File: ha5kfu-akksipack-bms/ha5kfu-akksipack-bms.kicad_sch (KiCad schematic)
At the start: 51 parts, among them IC2 BQ4050RSMR, J1 PACK, J2 PACK1, J3 PACK2, J4 COM, Q1 AON6512, Q2 AON6512, Q3 2N7002, Q4 AO3400A, Q5 AO3400A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

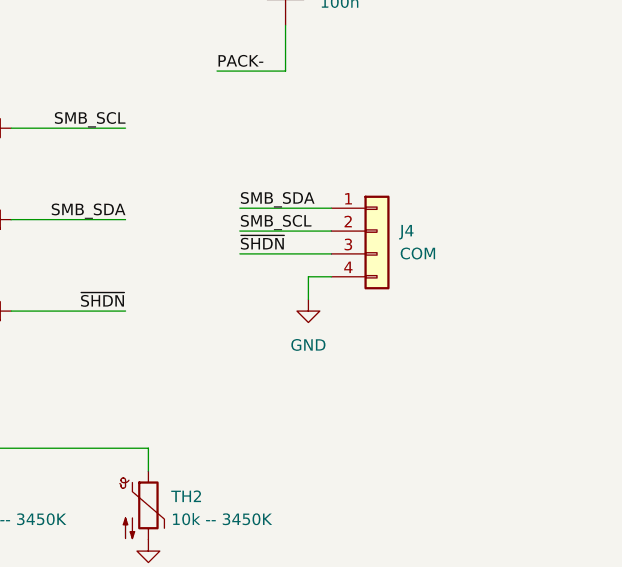
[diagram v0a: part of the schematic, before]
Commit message: Add pull-down for /SHDN
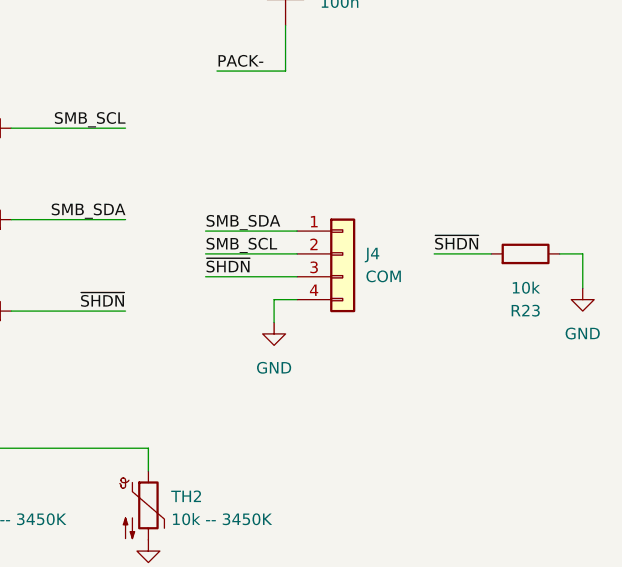
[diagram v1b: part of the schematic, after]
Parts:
- added R23: 10k, Resistor_SMD:R_0805_2012Metric_Pad1.20x1.40mm_HandSolder, symbol Device:R
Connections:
- net GND: now also R23.1
- net ~{SHDN}: now also R23.2
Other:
- moved on the sheet: J4
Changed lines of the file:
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@@
 	(wire
 		(pts
-			(xy 238.76 113.03) (xy 248.92 113.03)
+			(xy 234.95 115.57) (xy 245.11 115.57)
 		)
 		(stroke
@@
 	(wire
 		(pts
+			(xy 276.86 116.84) (xy 276.86 113.03)
+		)
+		(stroke
+			(width 0)
+			(type default)
+		)
+	)
+	(wire
+		(pts
 			(xy 36.83 73.66) (xy 36.83 91.44)
 		)
@@
 	(wire
 		(pts
-			(xy 246.38 118.11) (xy 246.38 115.57)
+			(xy 242.57 120.65) (xy 242.57 118.11)
 		)
 		(stroke
@@
 	(wire
 		(pts
+			(xy 266.7 113.03) (xy 260.35 113.03)
+		)
+		(stroke
+			(width 0)
+			(type default)
+		)
+	)
+	(wire
+		(pts
 			(xy 191.77 43.18) (xy 186.69 43.18)
 		)
@@
 	(wire
 		(pts
-			(xy 246.38 115.57) (xy 248.92 115.57)
+			(xy 242.57 118.11) (xy 245.11 118.11)
 		)
 		(stroke
@@
 	(wire
 		(pts
-			(xy 238.76 110.49) (xy 248.92 110.49)
+			(xy 234.95 113.03) (xy 245.11 113.03)
 		)
 		(stroke
@@
 	(wire
 		(pts
-			(xy 238.76 107.95) (xy 248.92 107.95)
+			(xy 234.95 110.49) (xy 245.11 110.49)
 		)
 		(stroke
@@
 	(wire
 		(pts
+			(xy 276.86 113.03) (xy 274.32 113.03)
+		)
+		(stroke
+			(width 0)
+			(type default)
+		)
+	)
+	(wire
+		(pts
 			(xy 90.17 111.76) (xy 90.17 119.38)
 		)
@@
 	)
 	(label "SMB_SCL"
-		(at 238.76 110.49 0)
+		(at 234.95 113.03 0)
 		(effects
 			(font
@@
 	)
 	(label "SMB_SDA"
-		(at 238.76 107.95 0)
+		(at 234.95 110.49 0)
 		(effects
 			(font
@@
 		)
 	)
+	(label "~{SHDN}"
+		(at 260.35 113.03 0)
+		(effects
+			(font
+				(size 1.27 1.27)
+			)
+			(justify left bottom)
+		)
+	)
 	(label "SMB_SDA"
 		(at 226.06 109.22 180)
@@
 	)
 	(label "~{SHDN}"
-		(at 238.76 113.03 0)
+		(at 234.95 115.57 0)
 		(effects
 			(font
@@
 	(symbol
 		(lib_id "power:GND")
-		(at 246.38 118.11 0)
+		(at 242.57 120.65 0)
 		(unit 1)
 		(exclude_from_sim no)
@@
 		(fields_autoplaced yes)
 		(property "Reference" "#PWR09"
-			(at 246.38 124.46 0)
+			(at 242.57 127 0)
 			(effects
 				(font
@@
 		)
 		(property "Value" "GND"
-			(at 246.38 123.19 0)
+			(at 242.57 125.73 0)
 			(effects
 				(font
@@
 		)
 		(property "Footprint" ""
-			(at 246.38 118.11 0)
+			(at 242.57 120.65 0)
 			(effects
 				(font
@@
 		)
 		(property "Datasheet" ""
-			(at 246.38 118.11 0)
+			(at 242.57 120.65 0)
 			(effects
 				(font
@@
 		)
 		(property "Description" "Power symbol creates a global label with name \"GND\" , ground"
-			(at 246.38 118.11 0)
+			(at 242.57 120.65 0)
 			(effects
 				(font
@@
 	)
 	(symbol
+		(lib_id "power:GND")
+		(at 276.86 116.84 0)
+		(mirror y)
+		(unit 1)
+		(exclude_from_sim no)
+		(in_bom yes)
+		(on_board yes)
+		(dnp no)
+		(fields_autoplaced yes)
+		(property "Reference" "#PWR010"
+			(at 276.86 123.19 0)
+			(effects
+				(font
+					(size 1.27 1.27)
+				)
+				(hide yes)
+			)
+		)
+		(property "Value" "GND"
+			(at 276.86 121.92 0)
+			(effects
+				(font
+					(size 1.27 1.27)
+				)
+			)
+		)
+		(property "Footprint" ""
+			(at 276.86 116.84 0)
+			(effects
+				(font
+					(size 1.27 1.27)
+				)
+				(hide yes)
+			)
+		)
+		(property "Datasheet" ""
+			(at 276.86 116.84 0)
+			(effects
+				(font
+					(size 1.27 1.27)
+				)
+				(hide yes)
+			)
+		)
+		(property "Description" "Power symbol creates a global label with name \"GND\" , ground"
+			(at 276.86 116.84 0)
+			(effects
+				(font
+					(size 1.27 1.27)
+				)
+				(hide yes)
+			)
+		)
+		(pin "1"
+		)
+		(instances
+			(project "ha5kfu-akksipack-bms"
+				(path "/9e1c3fa4-5fbe-43ed-babf-081bbfb08ec5"
+					(reference "#PWR010")
+					(unit 1)
+				)
+			)
+		)
+	)
+	(symbol
 		(lib_id "Device:D_Schottky")
 		(at 140.97 77.47 270)
@@
 	(symbol
 		(lib_id "Device:R")
+		(at 270.51 113.03 270)
+		(mirror x)
+		(unit 1)
+		(exclude_from_sim no)
+		(in_bom yes)
+		(on_board yes)
+		(dnp no)
+		(property "Reference" "R23"
+			(at 270.51 119.38 90)
+			(effects
+				(font
+					(size 1.27 1.27)
+				)
+			)
+		)
+		(property "Value" "10k"
+			(at 270.51 116.84 90)
+			(effects
+				(font
+					(size 1.27 1.27)
+				)
+			)
+		)
+		(property "Footprint" "Resistor_SMD:R_0805_2012Metric_Pad1.20x1.40mm_HandSolder"
+			(at 270.51 114.808 90)
+			(effects
+				(font
+					(size 1.27 1.27)
+				)
+				(hide yes)
+			)
+		)
+		(property "Datasheet" "~"
+			(at 270.51 113.03 0)
+			(effects
+				(font
+					(size 1.27 1.27)
+				)
+				(hide yes)
+			)
+		)
+		(property "Description" "Resistor"
+			(at 270.51 113.03 0)
+			(effects
+				(font
+					(size 1.27 1.27)
+				)
+				(hide yes)
+			)
+		)
+		(pin "1"
+		)
+		(pin "2"
+		)
+		(instances
+			(project "ha5kfu-akksipack-bms"
+				(path "/9e1c3fa4-5fbe-43ed-babf-081bbfb08ec5"
+					(reference "R23")
+					(unit 1)
+				)
+			)
+		)
+	)
+	(symbol
+		(lib_id "Device:R")
 		(at 64.77 55.88 0)
 		(unit 1)
@@
 	(symbol
 		(lib_id "Connector_Generic:Conn_01x04")
-		(at 254 110.49 0)
+		(at 250.19 113.03 0)
 		(unit 1)
 		(exclude_from_sim no)
@@
 		(fields_autoplaced yes)
 		(property "Reference" "J4"
-			(at 256.54 110.4899 0)
+			(at 252.73 113.0299 0)
 			(effects
 				(font
@@
 		)
 		(property "Value" "COM"
-			(at 256.54 113.0299 0)
+			(at 252.73 115.5699 0)
 			(effects
 				(font
@@
 		)
 		(property "Footprint" "Connector_PinHeader_2.54mm:PinHeader_1x04_P2.54mm_Vertical"
-			(at 254 110.49 0)
+			(at 250.19 113.03 0)
 			(effects
 				(font
@@
 		)
 		(property "Datasheet" "~"
-			(at 254 110.49 0)
+			(at 250.19 113.03 0)
 			(effects
 				(font
@@
 		)
 		(property "Description" "Generic connector, single row, 01x04, script generated (kicad-library-utils/schlib/autogen/connector/)"
-			(at 254 110.49 0)
+			(at 250.19 113.03 0)
 			(effects
 				(font

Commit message: Add initial PCB design
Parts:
- C1, C2, C3, C4, C5, C6, C7, C8: footprint Capacitor_SMD:C_0805_2012Metric_Pad1.18x1.45mm_HandSolder -> Capacitor_SMD:C_0603_1608Metric_Pad1.08x0.95mm_HandSolder
- C10: renamed from 100n1; value C -> 100n; footprint Capacitor_SMD:C_0805_2012Metric_Pad1.18x1.45mm_HandSolder -> Capacitor_SMD:C_0603_1608Metric_Pad1.08x0.95mm_HandSolder
- IC1: renamed from IC2; footprint BQ4050:QFN40P400X400X100-33N-D -> Package_DFN_QFN:VQFN-32-1EP_4x4mm_P0.4mm_EP2.8x2.8mm
- J1: footprint Connector_Wire:SolderWire-0.75sqmm_1x02_P4.8mm_D1.25mm_OD2.3mm -> Connector_AMASS:AMASS_XT30PW-M_1x02_P2.50mm_Horizontal
- J2, J3: footprint Connector_JST:JST_PH_B3B-PH-K_1x03_P2.00mm_Vertical -> Connector_JST:JST_PH_S3B-PH-K_1x03_P2.00mm_Horizontal
- R1, R10, R11, R13, R15, R16, R2, R3, R6, R7: footprint Resistor_SMD:R_0805_2012Metric_Pad1.20x1.40mm_HandSolder -> Resistor_SMD:R_0603_1608Metric_Pad0.98x0.95mm_HandSolder
- R12, R14, R17, R4, R5, R8, R9: footprint Resistor_SMD:R_1206_3216Metric -> Resistor_SMD:R_0603_1608Metric_Pad0.98x0.95mm_HandSolder
- R18: renamed from R23; footprint Resistor_SMD:R_0805_2012Metric_Pad1.20x1.40mm_HandSolder -> Resistor_SMD:R_0603_1608Metric_Pad0.98x0.95mm_HandSolder
- R19: renamed from R18; footprint Resistor_SMD:R_0805_2012Metric_Pad1.20x1.40mm_HandSolder -> Resistor_SMD:R_0603_1608Metric_Pad0.98x0.95mm_HandSolder
- R20: renamed from R19; footprint Resistor_SMD:R_1206_3216Metric -> Resistor_SMD:R_0603_1608Metric_Pad0.98x0.95mm_HandSolder
- R21: renamed from R20; footprint Resistor_SMD:R_1206_3216Metric -> Resistor_SMD:R_1206_3216Metric_Pad1.30x1.75mm_HandSolder
- R22: renamed from R21; footprint Resistor_SMD:R_0805_2012Metric_Pad1.20x1.40mm_HandSolder -> Resistor_SMD:R_0603_1608Metric_Pad0.98x0.95mm_HandSolder
- R23: renamed from R22; footprint Resistor_SMD:R_0805_2012Metric_Pad1.20x1.40mm_HandSolder -> Resistor_SMD:R_0603_1608Metric_Pad0.98x0.95mm_HandSolder
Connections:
- net GND: now also J3.1 (Pin_1); no longer J3.3 (Pin_3)
- net at BT2.2 (-), BT3.1 (+), Q5.2 (S)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: now also J2.1 (Pin_1), J3.3 (Pin_3); no longer J2.3 (Pin_3), J3.1 (Pin_1)
- net at BT1.1 (+), C1.1, D1.2 (A)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: now also J2.3 (Pin_3); no longer J2.1 (Pin_1)
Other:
- moved on the sheet: J2, J3

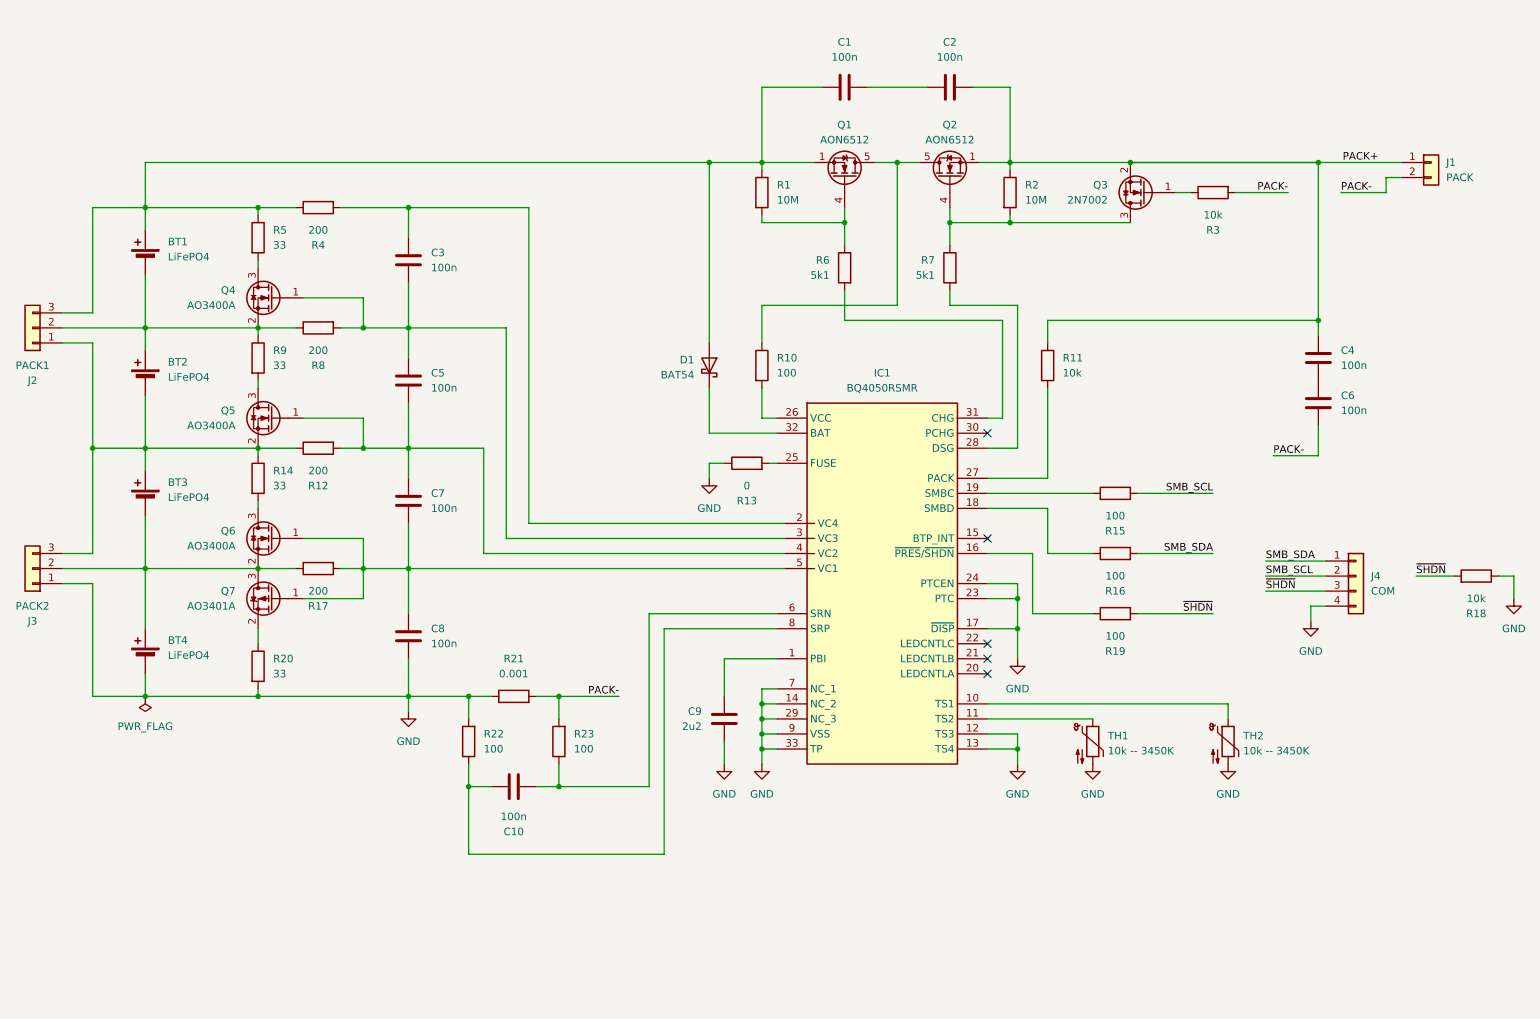
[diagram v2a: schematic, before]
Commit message: Add LEDs, modify PCB
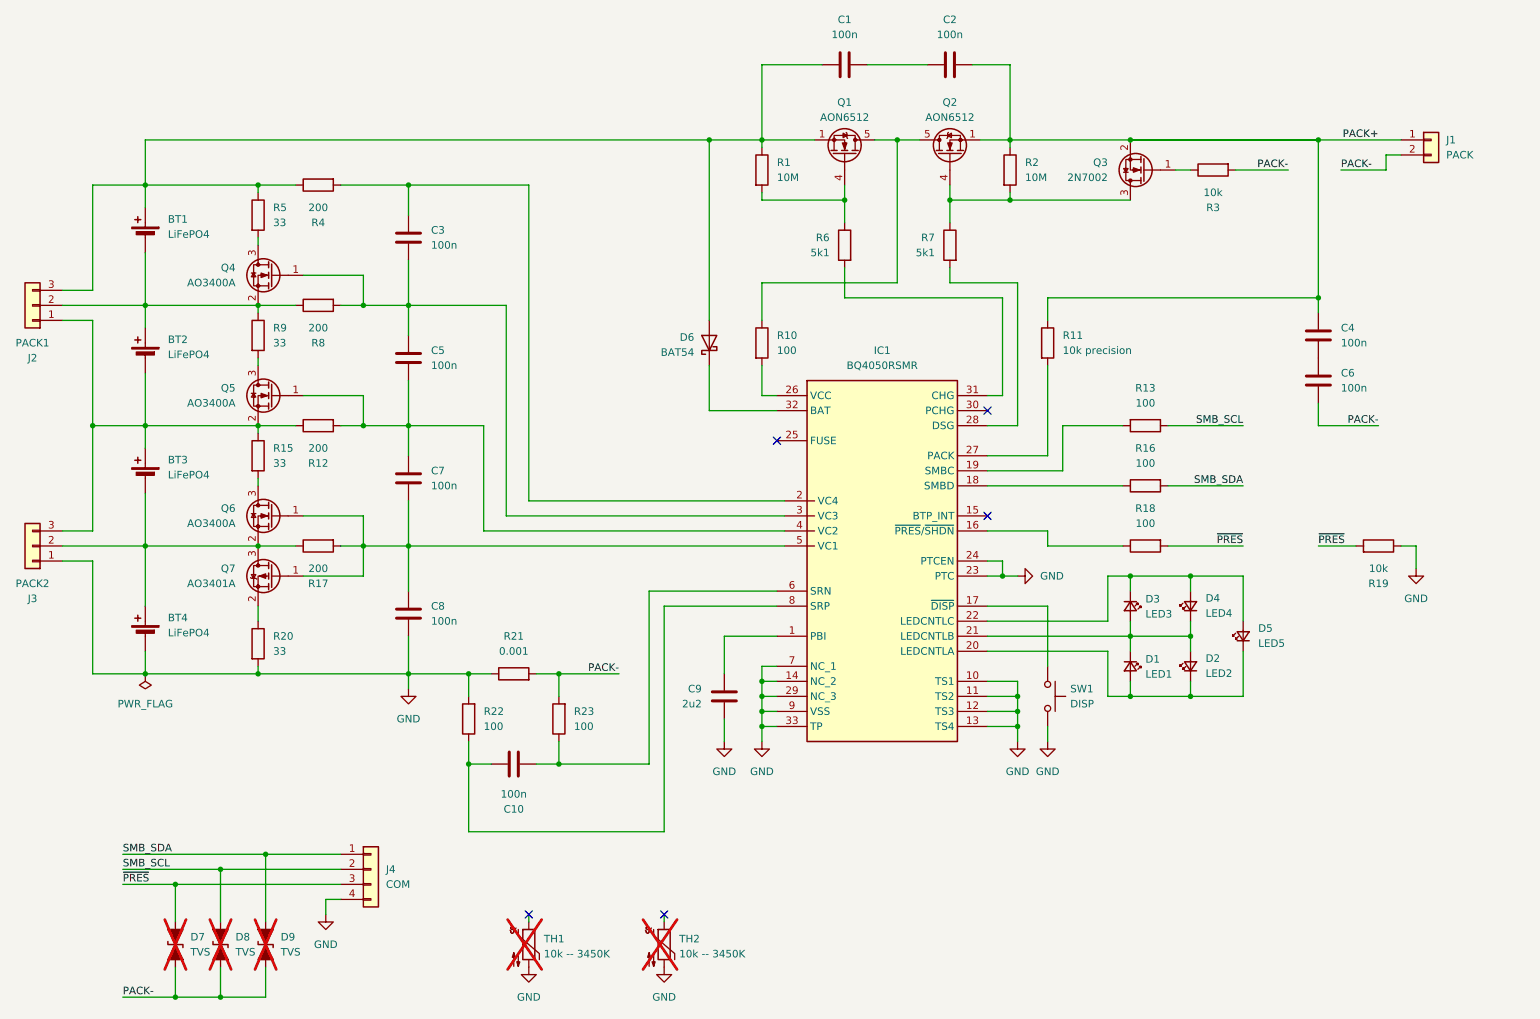
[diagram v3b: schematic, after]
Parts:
- removed D1: BAT54, Diode_SMD:D_SOD-323F, symbol Device:D_Schottky
- removed R13: 0, Resistor_SMD:R_0603_1608Metric_Pad0.98x0.95mm_HandSolder, symbol Device:R
- added D1: LED1, LED_SMD:LED_0603_1608Metric_Pad1.05x0.95mm_HandSolder, symbol Device:LED_Small
- added D2: LED2, LED_SMD:LED_0603_1608Metric_Pad1.05x0.95mm_HandSolder, symbol Device:LED_Small
- added D3: LED3, LED_SMD:LED_0603_1608Metric_Pad1.05x0.95mm_HandSolder, symbol Device:LED_Small
- added D4: LED4, LED_SMD:LED_0603_1608Metric_Pad1.05x0.95mm_HandSolder, symbol Device:LED_Small
- added D5: LED5, LED_SMD:LED_0603_1608Metric_Pad1.05x0.95mm_HandSolder, symbol Device:LED_Small
- added D6: BAT54, Diode_SMD:D_SOD-323F, symbol Diode:BAT54J
- added D7, D8, D9: TVS, symbol Device:D_TVS_Filled
- added SW1: DISP, Button_Switch_SMD:SW_SPST_TL3342, symbol Switch:SW_Push
- J1: footprint Connector_AMASS:AMASS_XT30PW-M_1x02_P2.50mm_Horizontal -> Connector_AMASS:AMASS_XT30U-F_1x02_P5.0mm_Vertical
- Q1, Q2: footprint Package_SO:PowerPAK_SO-8_Single -> Package_DFN_QFN:PQFN-8-EP_6x5mm_P1.27mm_Generic
- R11: value 10k -> 10k precision
- R15: renamed from R14; footprint Resistor_SMD:R_0603_1608Metric_Pad0.98x0.95mm_HandSolder -> Resistor_SMD:R_1206_3216Metric_Pad1.30x1.75mm_HandSolder
- R20, R5, R9: footprint Resistor_SMD:R_0603_1608Metric_Pad0.98x0.95mm_HandSolder -> Resistor_SMD:R_1206_3216Metric_Pad1.30x1.75mm_HandSolder
- TH1, TH2: now not fitted
- renumbered R15 to R13, R19 to R18, R18 to R19
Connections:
- net GND: now also IC1.10 (TS1), IC1.11 (TS2), SW1.2; no longer IC1.17 (~{DISP})
- net PACK-: now also D7.1 (A1), D8.1 (A1), D9.1 (A1)
- net SMB_SCL: now also D8.2 (A2)
- net SMB_SDA: now also D9.2 (A2)
- net at TH2.1: no longer IC1.10 (TS1)
- net at TH1.1: no longer IC1.11 (TS2)
- net at IC1.20 (LEDCNTLA): now also D1.2 (A), D2.1 (K), D5.1 (K)
- net at IC1.21 (LEDCNTLB): now also D1.1 (K), D2.2 (A), D3.2 (A), D4.1 (K)
- net at IC1.22 (LEDCNTLC): now also D3.1 (K), D4.2 (A), D5.2 (A)
- net at IC1.32 (BAT): now also D6.1 (K)
- net at BT1.1 (+), C1.1, J2.3 (Pin_3)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: now also D6.2 (A)
- net ~{SHDN} renamed ~{PRES}
- net ~{PRES}: now also D7.2 (A2)
- new net: IC1.17 (~{DISP}), SW1.1
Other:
- moved on the sheet: BT1, BT2, BT3, BT4, C1, C10, C2, C3, C4, C5, C6, C7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
